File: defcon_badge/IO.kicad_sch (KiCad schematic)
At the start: 10 parts, among them J30 SAO 2x3, J31 microSD, J32 UART debug, SW20 TS-1187A, SW21 TS-1187A, SW22 TS-1187A, SW23 TS-1187A

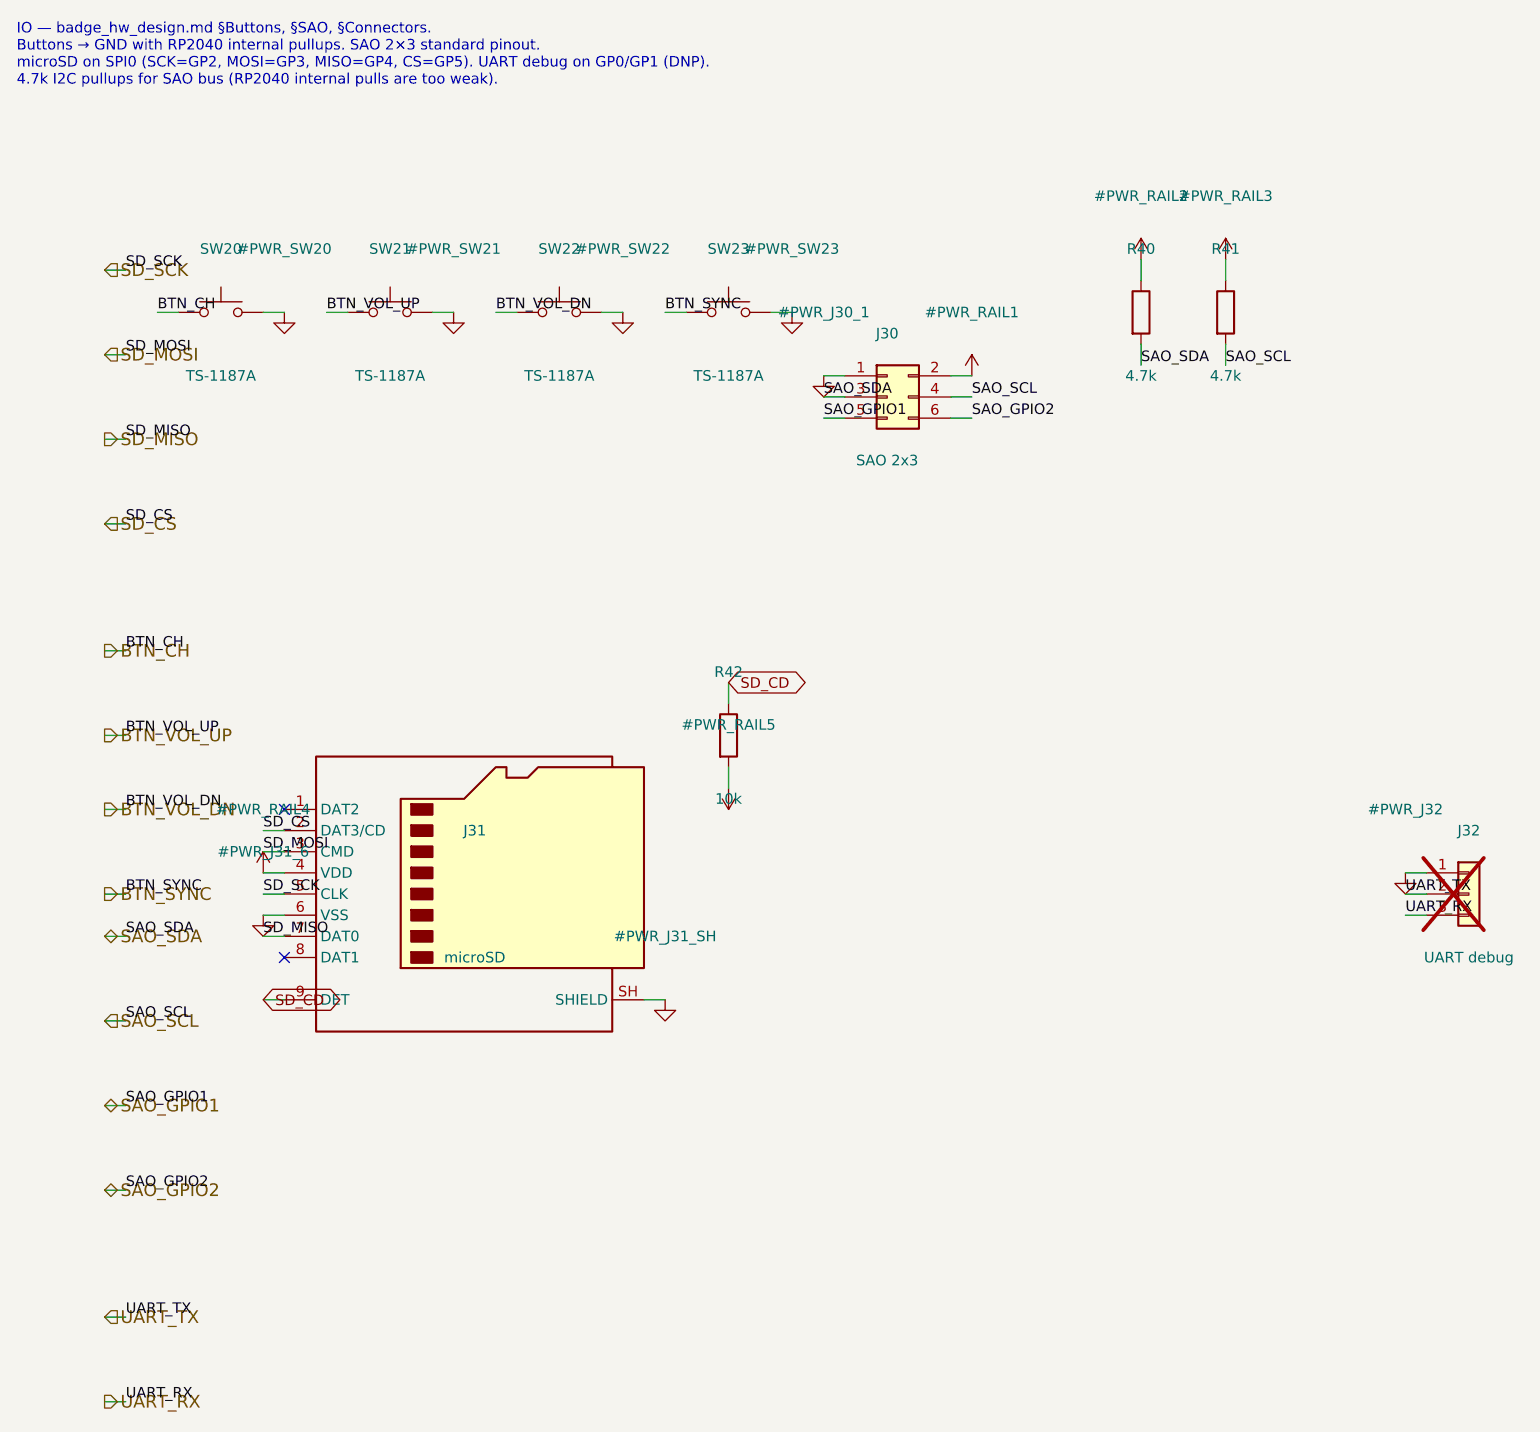
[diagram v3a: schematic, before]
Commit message: Schematic: remove unused J32/J33 debug headers (user request)
The UART debug header (J32, IO sheet) and SWD debug header (J33, MCU_Core)
are unused — the RP2040 is programmed via BOOTSEL/USB (TP1/TP2 pogo pads),
so neither was ever placed on the PCB. Removed both from the schematic so
schematic↔PCB parity stays clean.

Done via a new surgical tool (tools/remove_dev_headers.py) that deletes the
symbols, their power/labels/wires, and the cross-sheet UART plumbing (IO
hier-labels + top-sheet sheet pins + MCU_Core hier-labels/stubs) by
top-level S-expression element, preserving every other symbol UUID (so the
PCB footprint linkage is untouched — no re-sync needed).

The RP2040 debug pins (SWCLK/SWDIO) and UART pins (GP0/GP1) keep their
labels as documented single-pin nets so future test points can attach.

Verified: kicad-cli ERC 0 errors, schematic parity 0 issues. Net warning
delta vs baseline: +4 isolated_pin_label (the intended documented debug
pins), -2 endpoint_off_grid; everything else unchanged.

Co-Authored-By: Claude Opus 4.8 (1M context) <noreply@anthropic.com>
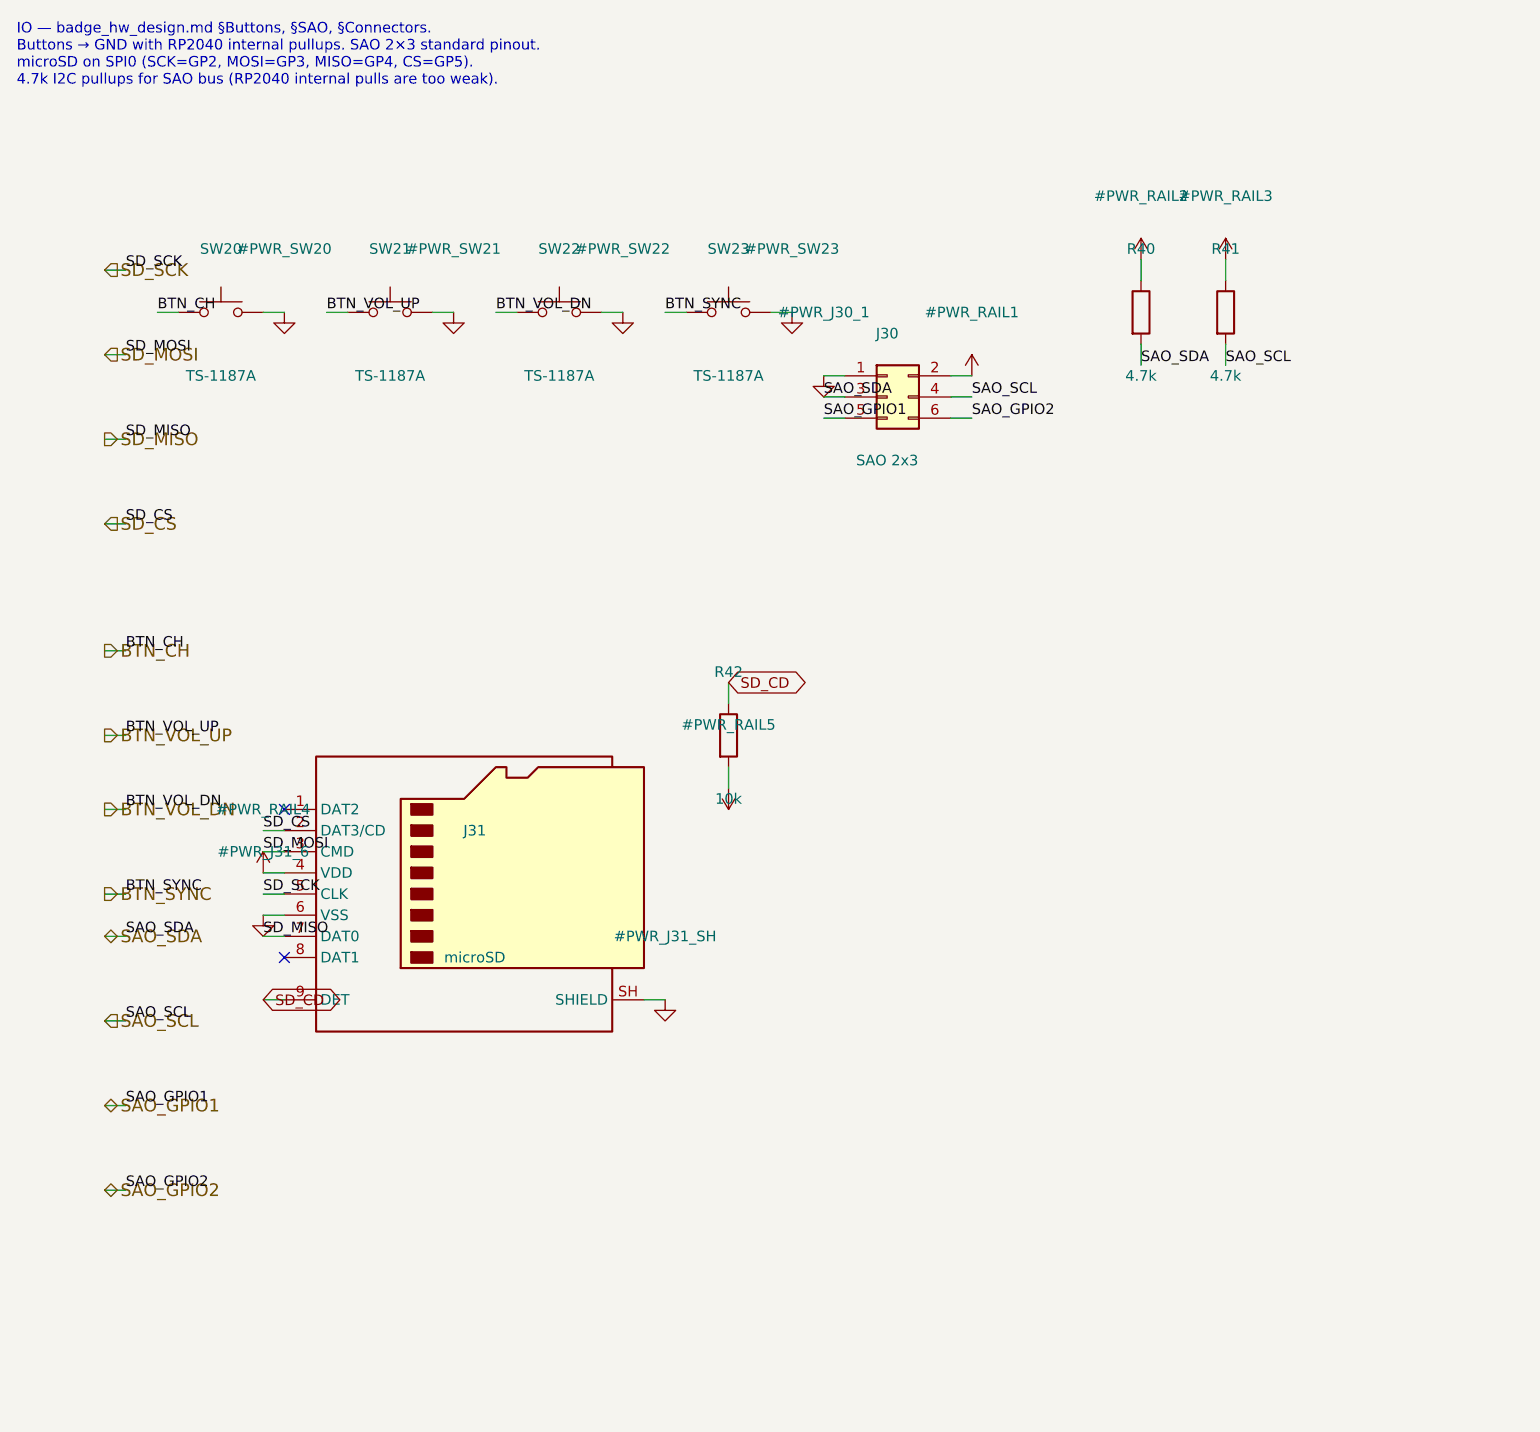
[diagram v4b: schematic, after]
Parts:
- removed J32: UART debug, Connector_PinHeader_2.54mm:PinHeader_1x03_P2.54mm_Vertical, symbol Connector_Generic:Conn_01x03
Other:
- note added: "IO — badge_hw_design.md §Buttons, §SAO, §Connectors. Buttons → GND with RP2040 internal pullups. SAO 2×3 standard pinout. microSD on SPI0 (SCK=GP2, MOSI=GP3, MISO=GP4, CS=GP5). 4.7k I2C pullups for SAO bus (RP2040 internal pulls are too weak)."
- note removed: "IO — badge_hw_design.md §Buttons, §SAO, §Connectors. Buttons → GND with RP2040 internal pullups. SAO 2×3 standard pinout. microSD on SPI0 (SCK=GP2, MOSI=GP3, MISO=GP4, CS=GP5). UART debug on GP0/GP1 (DNP). 4.7k I2C pullups for SAO bus (RP2040 internal pulls are too weak)."
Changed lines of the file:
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@@
 		(comment 1 "3× TS-1187A tactile (CH / VOL+ / VOL−) via internal RP2040 pullups")
 		(comment 2 "Standard SAO v1.69 2×3 (3V3 / GND / SDA / SCL / GP1 / GP2), 4.7k SAO_SDA/SCL pullups")
-		(comment 3 "microSD push socket on SPI0; debug UART 1×3 header (DNP)")
-	)
-	(text "IO — badge_hw_design.md §Buttons, §SAO, §Connectors.\nButtons → GND with RP2040 internal pullups. SAO 2×3 standard pinout.\nmicroSD on SPI0 (SCK=GP2, MOSI=GP3, MISO=GP4, CS=GP5). UART debug on GP0/GP1 (DNP).\n4.7k I2C pullups for SAO bus (RP2040 internal pulls are too weak)." (exclude_from_sim no) (at 25.00 25.00 0) (effects (font (size 1.27 1.27)) (justify left top)))
+		(comment 3 "microSD push socket on SPI0")
+	)
+	(text "IO — badge_hw_design.md §Buttons, §SAO, §Connectors.\nButtons → GND with RP2040 internal pullups. SAO 2×3 standard pinout.\nmicroSD on SPI0 (SCK=GP2, MOSI=GP3, MISO=GP4, CS=GP5).\n4.7k I2C pullups for SAO bus (RP2040 internal pulls are too weak)." (exclude_from_sim no) (at 25.00 25.00 0) (effects (font (size 1.27 1.27)) (justify left top)))
 	(symbol
 		(lib_id "Switch:SW_Push")
@@
 				(path "/8c0b3d8b-46d3-4173-ab1e-a61765f77d61/608539de-722a-4bca-b1da-2c313b60cd6f"
 					(reference "#PWR_RAIL5")
-					(unit 1)
-				)
-			)
-		)
-	)
-	(symbol
-		(lib_id "Connector_Generic:Conn_01x03")
-		(at 199.39 129.54 0)
-		(unit 1)
-		(body_style 1)
-		(exclude_from_sim no)
-		(in_bom yes)
-		(on_board yes)
-		(in_pos_files yes)
-		(dnp yes)
-		(fields_autoplaced yes)
-		(property "Reference" "J32" (at 199.39 121.92 0) (effects (font (size 1.27 1.27))))
-		(property "Value" "UART debug" (at 199.39 137.16 0) (effects (font (size 1.27 1.27))))
-		(property "Footprint" "Connector_PinHeader_2.54mm:PinHeader_1x03_P2.54mm_Vertical" (at 199.39 129.54 0) (show_name no) (hide yes) (effects (font (size 1.27 1.27))))
-		(property "Datasheet" "" (at 199.39 129.54 0) (show_name no) (hide yes) (effects (font (size 1.27 1.27))))
-		(property "Description" "Debug UART header (DNP — pads laid out, header not stuffed)" (at 199.39 129.54 0) (show_name no) (hide yes) (effects (font (size 1.27 1.27))))
-		(pin "1")
-		(pin "2")
-		(pin "3")
-		(instances
-			(project "defcon_badge"
-				(path "/8c0b3d8b-46d3-4173-ab1e-a61765f77d61/608539de-722a-4bca-b1da-2c313b60cd6f"
-					(reference "J32")
-					(unit 1)
-				)
-			)
-		)
-	)
-	(symbol
-		(lib_id "power:GND")
-		(at 191.77 127.00 0)
-		(unit 1)
-		(body_style 1)
-		(exclude_from_sim no)
-		(in_bom yes)
-		(on_board yes)
-		(in_pos_files yes)
-		(dnp no)
-		(fields_autoplaced yes)
-		(property "Reference" "#PWR_J32" (at 191.77 119.38 0) (effects (font (size 1.27 1.27))))
-		(property "Value" "GND" (at 191.77 134.62 0) (effects (font (size 1.27 1.27)) (hide yes)))
-		(property "Footprint" "" (at 191.77 127.00 0) (show_name no) (hide yes) (effects (font (size 1.27 1.27))))
-		(property "Datasheet" "" (at 191.77 127.00 0) (show_name no) (hide yes) (effects (font (size 1.27 1.27))))
-		(property "Description" "" (at 191.77 127.00 0) (show_name no) (hide yes) (effects (font (size 1.27 1.27))))
-		(pin "1")
-		(instances
-			(project "defcon_badge"
-				(path "/8c0b3d8b-46d3-4173-ab1e-a61765f77d61/608539de-722a-4bca-b1da-2c313b60cd6f"
-					(reference "#PWR_J32")
 					(unit 1)
 				)
@@
 	(wire (pts (xy 110.49 106.68) (xy 110.49 104.14)) (stroke (width 0) (type default)))
 	(wire (pts (xy 110.49 114.30) (xy 110.49 116.84)) (stroke (width 0) (type default)))
-	(wire (pts (xy 194.31 127.00) (xy 191.77 127.00)) (stroke (width 0) (type default)))
-	(wire (pts (xy 194.31 129.54) (xy 191.77 129.54)) (stroke (width 0) (type default)))
-	(wire (pts (xy 194.31 132.08) (xy 191.77 132.08)) (stroke (width 0) (type default)))
 	(wire (pts (xy 35.56 54.61) (xy 38.10 54.61)) (stroke (width 0) (type default)))
 	(wire (pts (xy 35.56 64.77) (xy 38.10 64.77)) (stroke (width 0) (type default)))
@@
 	(wire (pts (xy 35.56 154.94) (xy 38.10 154.94)) (stroke (width 0) (type default)))
 	(wire (pts (xy 35.56 165.10) (xy 38.10 165.10)) (stroke (width 0) (type default)))
-	(wire (pts (xy 35.56 180.34) (xy 38.10 180.34)) (stroke (width 0) (type default)))
-	(wire (pts (xy 35.56 190.50) (xy 38.10 190.50)) (stroke (width 0) (type default)))
 	(no_connect (at 57.15 119.38))
 	(no_connect (at 57.15 137.16))
@@
 	(label "SD_SCK" (at 54.61 129.54 0) (effects (font (size 1.27 1.27)) (justify left bottom)))
 	(label "SD_MISO" (at 54.61 134.62 0) (effects (font (size 1.27 1.27)) (justify left bottom)))
-	(label "UART_TX" (at 191.77 129.54 0) (effects (font (size 1.27 1.27)) (justify left bottom)))
-	(label "UART_RX" (at 191.77 132.08 0) (effects (font (size 1.27 1.27)) (justify left bottom)))
 	(label "SD_SCK" (at 38.10 54.61 0) (effects (font (size 1.27 1.27)) (justify left bottom)))
 	(label "SD_MOSI" (at 38.10 64.77 0) (effects (font (size 1.27 1.27)) (justify left bottom)))
@@
 	(label "SAO_GPIO1" (at 38.10 154.94 0) (effects (font (size 1.27 1.27)) (justify left bottom)))
 	(label "SAO_GPIO2" (at 38.10 165.10 0) (effects (font (size 1.27 1.27)) (justify left bottom)))
-	(label "UART_TX" (at 38.10 180.34 0) (effects (font (size 1.27 1.27)) (justify left bottom)))
-	(label "UART_RX" (at 38.10 190.50 0) (effects (font (size 1.27 1.27)) (justify left bottom)))
 	(hierarchical_label "SD_SCK" (shape input) (at 35.56 54.61 0) (effects (font (size 1.524 1.524)) (justify left)))
 	(hierarchical_label "SD_MOSI" (shape input) (at 35.56 64.77 0) (effects (font (size 1.524 1.524)) (justify left)))
@@
 	(hierarchical_label "SAO_GPIO1" (shape bidirectional) (at 35.56 154.94 0) (effects (font (size 1.524 1.524)) (justify left)))
 	(hierarchical_label "SAO_GPIO2" (shape bidirectional) (at 35.56 165.10 0) (effects (font (size 1.524 1.524)) (justify left)))
-	(hierarchical_label "UART_TX" (shape input) (at 35.56 180.34 0) (effects (font (size 1.524 1.524)) (justify left)))
-	(hierarchical_label "UART_RX" (shape output) (at 35.56 190.50 0) (effects (font (size 1.524 1.524)) (justify left)))
 	(global_label "SD_CD" (shape bidirectional) (at 54.61 142.24 0) (effects (font (size 1.27 1.27)) (justify left)))
 	(global_label "SD_CD" (shape bidirectional) (at 110.49 104.14 0) (effects (font (size 1.27 1.27)) (justify left)))
